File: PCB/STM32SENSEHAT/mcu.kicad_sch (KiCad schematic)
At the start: 3 parts, among them J2 Conn_01x24_Socket, J3 Conn_01x24_Socket, J6 Conn_01x10_Pin

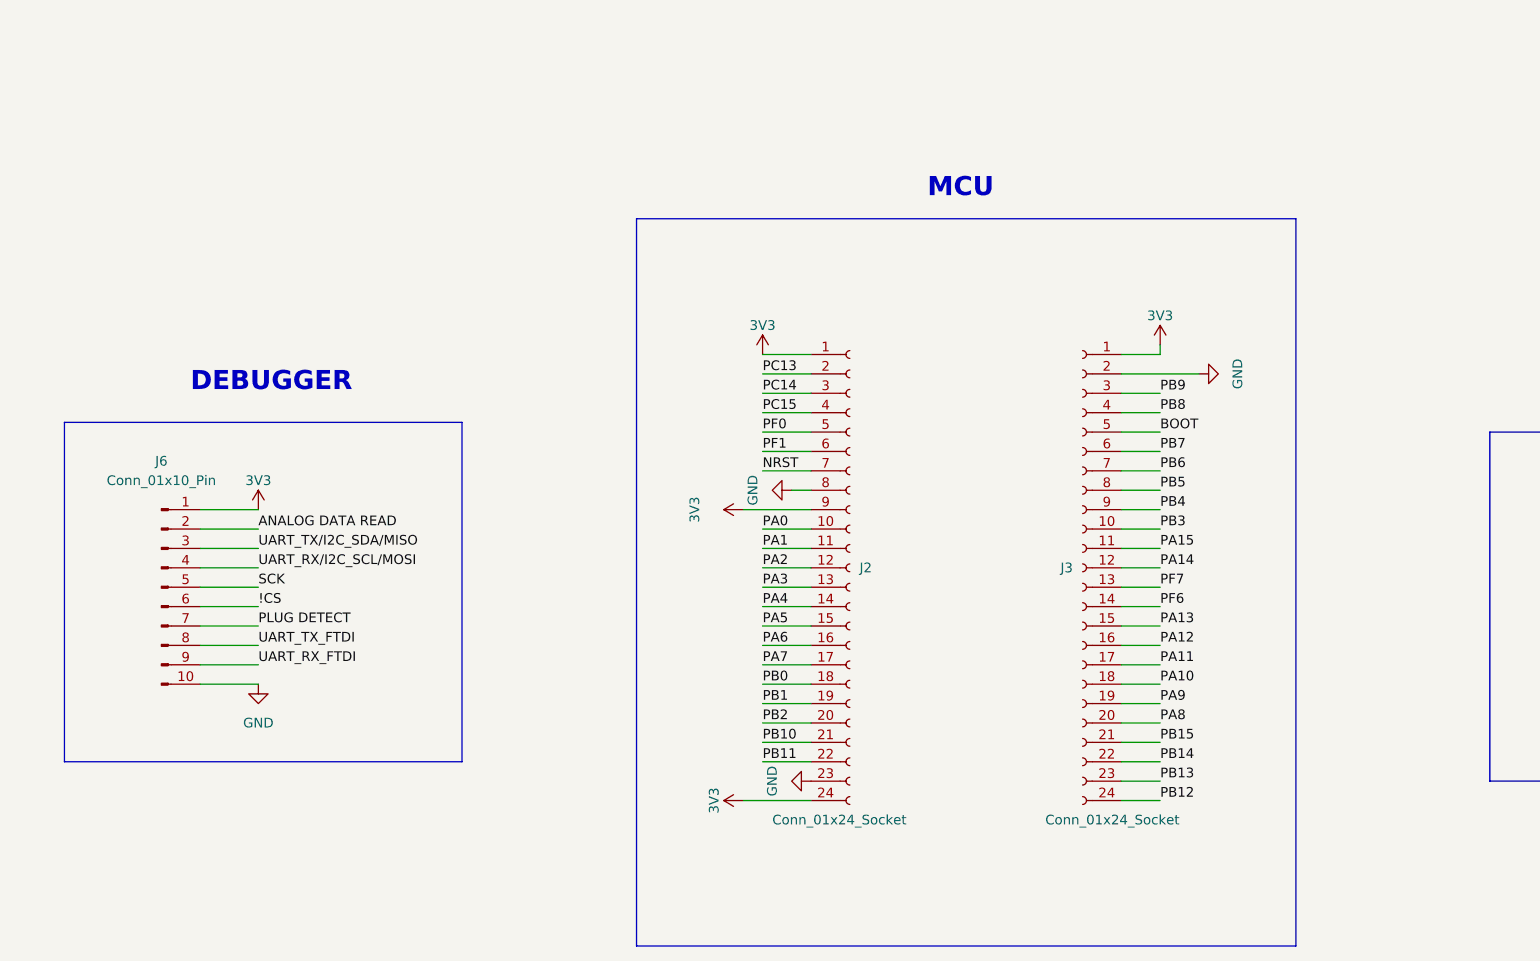
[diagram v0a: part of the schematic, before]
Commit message: Removed the extra sensor, Modified BME280 interfacing and FTDI UART pins. Added Manual Reset to MCU and configured BOOT pin
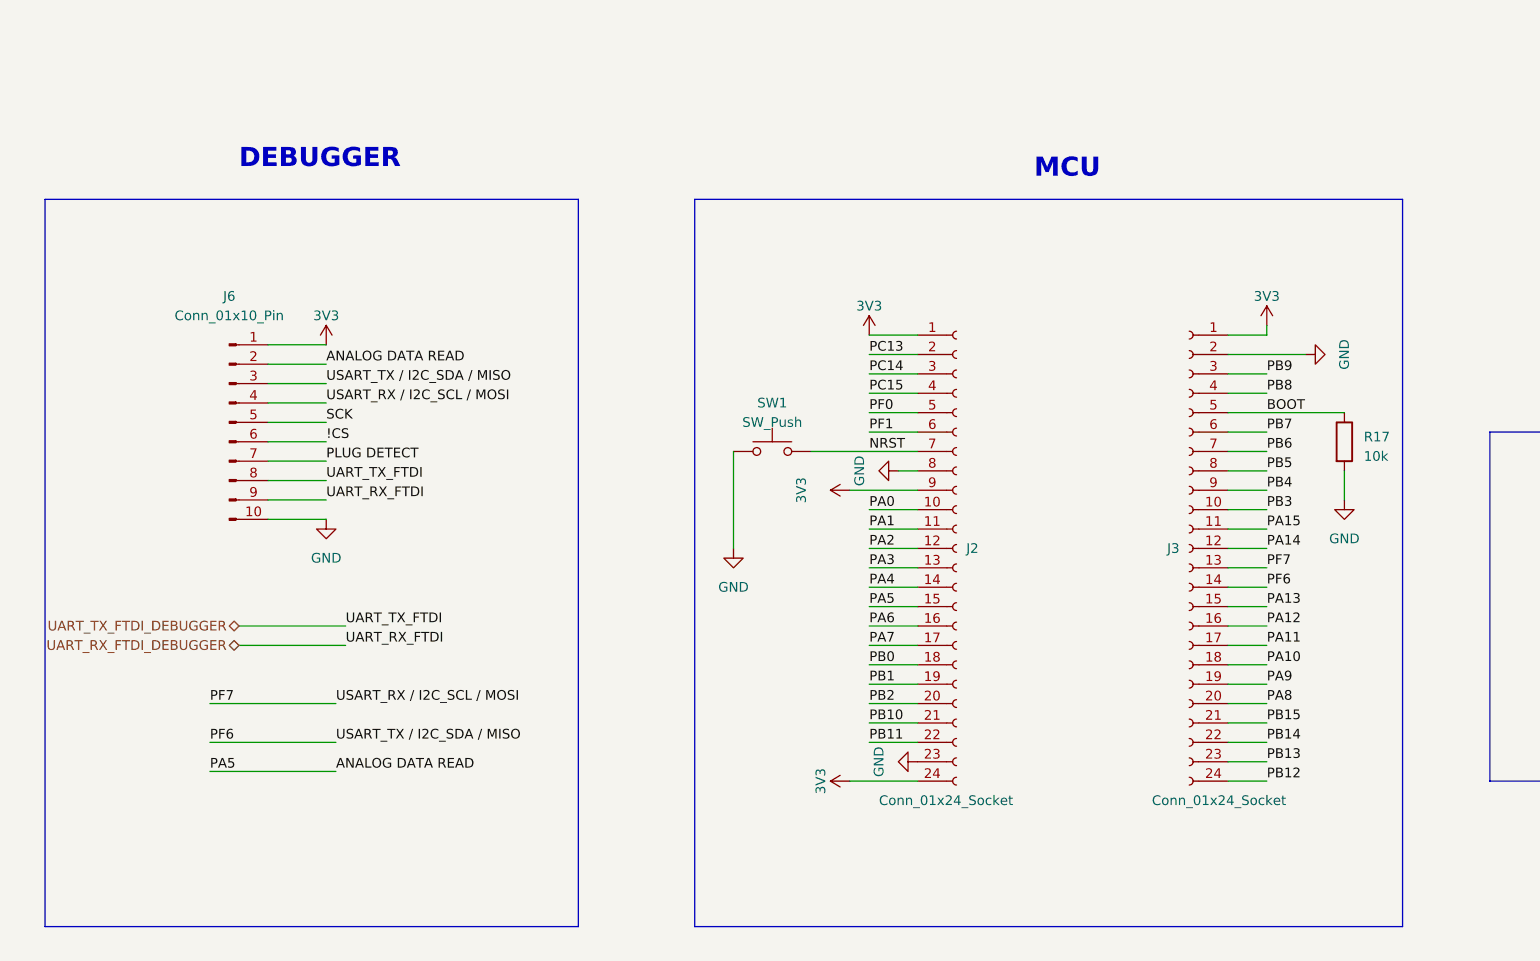
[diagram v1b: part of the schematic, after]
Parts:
- added R17: 10k, symbol Device:R
- added SW1: SW_Push, symbol Switch:SW_Push
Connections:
- net ANALOG DATA READ is gone; now on net PA5: J6.2 (Pin_2)
- net UART_RX/I2C_SCL/MOSI is gone; now on net STM_I2C_SCL: J6.4 (Pin_4)
- net UART_TX/I2C_SDA/MISO is gone; now on net STM_I2C_SDA: J6.3 (Pin_3)
- net BOOT: now also R17.1
- net GND: now also R17.2, SW1.1
- net NRST: now also SW1.2
- net UART_RX_FTDI renamed UART_RX_FTDI_DEBUGGER
- net UART_TX_FTDI renamed UART_TX_FTDI_DEBUGGER
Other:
- moved on the sheet: J2, J3, J6

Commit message: Revised schematics. Moved USB and EEPROM sub modules to MCU sheet and and rectified the top sheet accordingly
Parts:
- added C1, C2: 47pF, symbol Device:C_Small
- added C3: 10nF, symbol Device:C_Small
- added C4, C5: 100nF, symbol Device:C_Small
- added C6: 4.7uF, symbol Device:C_Small
- added FB1: FerriteBead, symbol Device:FerriteBead
- added J1: USB_B_Micro, symbol Connector:USB_B_Micro
- added J7: Conn_01x05_Pin, symbol Connector:Conn_01x05_Pin
- added R13, R16: 1.5k, symbol Device:R
- added R2, R3: 27R, symbol Device:R_Small
- added U3: FT230XQ, Package_DFN_QFN:QFN-16-1EP_4x4mm_P0.65mm_EP2.1x2.1mm, symbol Interface_USB:FT230XQ
- added U6: CAT24C256, symbol Memory_EEPROM:CAT24C256
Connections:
- net UART_RX_FTDI_DEBUGGER is gone; now on net PA10: J6.9 (Pin_9)
- net UART_TX_FTDI_DEBUGGER is gone; now on net PA9: J6.8 (Pin_8)
- net GND: now also C1.2, C2.2, C3.2, C4.2, C5.2, C6.2, J1.4 (ID), J1.5 (GND), J1.6 (Shield), J7.4 (Pin_4), J7.5 (Pin_5), U3.13 (GND), U3.17 (GND), U3.3 (GND), U6.1 (A0), U6.2 (A1), U6.3 (A2), U6.4 (GND), U6.7 (WP)
- net STM_I2C_SCL: now also R16.2, U6.6 (SCL)
- net STM_I2C_SDA: now also R13.2, U6.5 (SDA)
- net VCC: now also C3.1, C5.1, C6.1, FB1.1, FB1.2, J1.1 (VBUS), J7.1 (Pin_1), R13.1, R16.1, U3.10 (VCC), U6.8 (VCC)
- net STM_UART_RX renamed PA9
- net PA9: now also U3.15 (TXD)
- net STM_UART_TX renamed PA10
- net PA10: now also U3.2 (RXD)
- new net: C4.1, U3.1 (VCCIO), U3.8 (3V3OUT), U3.9 (~{RESET})
- new net: R3.2, U3.7 (USBDM)
- new net: R2.2, U3.6 (USBDP)
- new net CTS: U3.4 (~{CTS})
- new net D+: C2.1, J1.3 (D+), J7.3 (Pin_3), R2.1
- new net D-: C1.1, J1.2 (D-), J7.2 (Pin_2), R3.1
- new net RTS: U3.16 (~{RTS})
- no-connect marks 0 -> 4
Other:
- note added: "MEMORY"
- note added: "USB-FTDI INTERFACE"

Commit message: Added extra set of male pin headers
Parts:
- added J5, J8: Conn_01x24_Pin, symbol Connector:Conn_01x24_Pin
- added J7: Conn_01x04_Socket, symbol Connector:Conn_01x04_Socket
- added J9: Conn_01x05_Socket, symbol Connector:Conn_01x05_Socket
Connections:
- net BOOT: now also J5.5 (Pin_5)
- net GND: now also J5.2 (Pin_2), J8.23 (Pin_23), J8.8 (Pin_8), J9.5 (Pin_5)
- net NRST: now also J7.1 (Pin_1), J8.7 (Pin_7)
- net PA0: now also J8.10 (Pin_10)
- net PA1: now also J8.11 (Pin_11)
- net PA10: now also J5.18 (Pin_18)
- net PA11: now also J5.17 (Pin_17)
- net PA12: now also J5.16 (Pin_16)
- net PA13: now also J5.15 (Pin_15), J7.3 (Pin_3)
- net PA14: now also J5.12 (Pin_12), J7.2 (Pin_2)
- net PA15: now also J5.11 (Pin_11)
- net PA2: now also J8.12 (Pin_12)
- net PA3: now also J8.13 (Pin_13)
- net PA4: now also J8.14 (Pin_14)
- net PA5: now also J8.15 (Pin_15)
- net PA6: now also J8.16 (Pin_16)
- net PA7: now also J8.17 (Pin_17)
- net PA8: now also J5.20 (Pin_20)
- net PA9: now also J5.19 (Pin_19)
- net PB0: now also J8.18 (Pin_18)
- net PB1: now also J8.19 (Pin_19)
- net PB10: now also J8.21 (Pin_21)
- net PB11: now also J8.22 (Pin_22)
- net PB12: now also J5.24 (Pin_24)
- net PB13: now also J5.23 (Pin_23)
- net PB14: now also J5.22 (Pin_22)
- net PB15: now also J5.21 (Pin_21)
- net PB2: now also J8.20 (Pin_20)
- net PB3: now also J5.10 (Pin_10)
- net PB4: now also J5.9 (Pin_9)
- net PB5: now also J5.8 (Pin_8)
- net PB6: now also J5.7 (Pin_7)
- net PB7: now also J5.6 (Pin_6)
- net PB8: now also J5.4 (Pin_4)
- net PB9: now also J5.3 (Pin_3)
- net PC13: now also J8.2 (Pin_2)
- net PC14: now also J8.3 (Pin_3)
- net PC15: now also J8.4 (Pin_4)
- net PF0: now also J8.5 (Pin_5)
- net PF1: now also J8.6 (Pin_6)
- net STM_I2C_SCL: now also J5.13 (Pin_13)
- net STM_I2C_SDA: now also J5.14 (Pin_14)
- net VCC: now also J9.1 (Pin_1), J9.2 (Pin_2)
- net D+ renamed USB_DP
- net USB_DP: now also J9.3 (Pin_3)
- net D- renamed USB_DN
- net USB_DN: now also J9.4 (Pin_4)
- new net VBAT: J8.1 (Pin_1)
- new net VDD: J5.1 (Pin_1), J8.24 (Pin_24)
- new net VDDA: J8.9 (Pin_9)
- no-connect marks 4 -> 5
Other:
- note added: "TEST-P0INTS"
- moved on the sheet: C1, C2, C3, C4, C5, C6, FB1, J1, J2, J3, J6, J7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

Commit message: Protectuion features added to all schematica
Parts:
- added R14 (x2): 0R, symbol Device:R_Small
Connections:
- net STM_I2C_SCL: now also R14.2; no longer U6.6 (SCL)
- net STM_I2C_SDA: now also R14.1; no longer R13.2
- net VCC: no longer C3.1, FB1.2, J1.1 (VBUS), J2.1 (Pin_1), J2.24 (Pin_24), J2.9 (Pin_9), J3.1 (Pin_1), J6.1 (Pin_1), J7.1 (Pin_1), J9.1 (Pin_1), J9.2 (Pin_2), R13.1, R16.1, U6.8 (VCC)
- net CTS: no longer names the net of U3.4 (~{CTS})
- net RTS: no longer names the net of U3.16 (~{RTS})
- new net: R14.1, U6.6 (SCL)
- new net: R13.2, R14.2
- new net +5V: C3.1, FB1.2, J1.1 (VBUS), J7.1 (Pin_1), J9.1 (Pin_1)
- new net 3V3: J2.1 (Pin_1), J2.24 (Pin_24), J2.9 (Pin_9), J3.1 (Pin_1), J6.1 (Pin_1), J9.2 (Pin_2), R13.1, R16.1, U6.8 (VCC)
- no-connect marks 5 -> 7
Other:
- moved on the sheet: J2, J3, J5, J6, J7, J8, J9, R13, R16, R17, SW1, U6

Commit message: Schematics reviewed
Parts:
- J2, J3, J5, J8: footprint (none) -> Connector_PinHeader_2.54mm:PinHeader_1x24_P2.54mm_Vertical
- J6: footprint (none) -> Connector_PinHeader_2.54mm:PinHeader_1x10_P2.54mm_Vertical
- J7: footprint (none) -> Connector_PinHeader_2.54mm:PinHeader_1x04_P2.54mm_Vertical
- J7, J9: footprint (none) -> Connector_PinHeader_2.54mm:PinHeader_1x05_P2.54mm_Vertical
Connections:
- net VCC is gone; now on net +5V: C5.1, C6.1, FB1.1, U3.10 (VCC)
- net +5V: no longer C3.1, FB1.2, J1.1 (VBUS), J7.1 (Pin_1)
- net PB12 renamed STM32_CS
- net PB13 renamed STM32_SCLK
- net PB14 renamed STM32_MISO
- net PB15 renamed STM32_MOSI
- new net VBUS: C3.1, FB1.2, J1.1 (VBUS), J7.1 (Pin_1)

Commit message: Added footprints to the components but still pending review by Rumbizdai and Phomolo
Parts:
- C1, C2, C3, C4, C5, C6: footprint (none) -> Capacitor_SMD:C_0805_2012Metric
- FB1, R2, R3: footprint (none) -> Resistor_SMD:R_0603_1608Metric
- J1: footprint (none) -> Connector_USB:USB_Micro-AB_Molex_47590-0001
- J2, J3: footprint Connector_PinHeader_2.54mm:PinHeader_1x24_P2.54mm_Vertical -> Connector_PinSocket_2.54mm:PinSocket_1x24_P2.54mm_Vertical
- J7: footprint Connector_PinHeader_2.54mm:PinHeader_1x04_P2.54mm_Vertical -> Connector_PinSocket_2.54mm:PinSocket_1x04_P2.54mm_Vertical
- J9: footprint Connector_PinHeader_2.54mm:PinHeader_1x05_P2.54mm_Vertical -> Connector_PinSocket_2.54mm:PinSocket_1x05_P2.54mm_Vertical
- R13, R14, R16, R17: footprint (none) -> Resistor_SMD:R_0805_2012Metric
- SW1: footprint (none) -> Button_Switch_THT:SW_PUSH_6mm
- U6: footprint (none) -> Package_SO:SOIC-8-1EP_3.9x4.9mm_P1.27mm_EP2.41x3.3mm
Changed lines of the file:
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@@
       (effects (font (size 1.27 1.27)) (justify left))
     )
-    (property "Footprint" "Connector_PinHeader_2.54mm:PinHeader_1x24_P2.54mm_Vertical" (at 240.03 64.77 0)
+    (property "Footprint" "Connector_PinSocket_2.54mm:PinSocket_1x24_P2.54mm_Vertical" (at 240.03 64.77 0)
       (effects (font (size 1.27 1.27)) hide)
     )
@@
       (effects (font (size 1.27 1.27)) (justify left))
     )
-    (property "Footprint" "Connector_PinHeader_2.54mm:PinHeader_1x05_P2.54mm_Vertical" (at 118.11 64.77 0)
+    (property "Footprint" "Connector_PinSocket_2.54mm:PinSocket_1x05_P2.54mm_Vertical" (at 118.11 64.77 0)
       (effects (font (size 1.27 1.27)) hide)
     )
@@
       (effects (font (size 1.27 1.27)))
     )
-    (property "Footprint" "" (at 38.1 153.67 0)
+    (property "Footprint" "Connector_USB:USB_Micro-AB_Molex_47590-0001" (at 38.1 153.67 0)
       (effects (font (size 1.27 1.27)) hide)
     )
@@
       (effects (font (size 1.27 1.27)) (justify left))
     )
-    (property "Footprint" "" (at 258.572 50.8 90)
+    (property "Footprint" "Resistor_SMD:R_0805_2012Metric" (at 258.572 50.8 90)
       (effects (font (size 1.27 1.27)) hide)
     )
@@
       (effects (font (size 1.27 1.27)) (justify left))
     )
-    (property "Footprint" "" (at 92.71 182.88 0)
+    (property "Footprint" "Capacitor_SMD:C_0805_2012Metric" (at 92.71 182.88 0)
       (effects (font (size 1.27 1.27)) hide)
     )
@@
       (effects (font (size 1.27 1.27)) (justify left))
     )
-    (property "Footprint" "" (at 69.85 154.94 0)
+    (property "Footprint" "Resistor_SMD:R_0603_1608Metric" (at 69.85 154.94 0)
       (effects (font (size 1.27 1.27)) hide)
     )
@@
       (effects (font (size 1.27 1.27)))
     )
-    (property "Footprint" "" (at 355.6 66.04 0)
+    (property "Footprint" "Resistor_SMD:R_0805_2012Metric" (at 355.6 66.04 0)
       (effects (font (size 1.27 1.27)) hide)
     )
@@
       (effects (font (size 1.27 1.27)) (justify left))
     )
-    (property "Footprint" "" (at 332.74 66.04 0)
+    (property "Footprint" "Package_SO:SOIC-8-1EP_3.9x4.9mm_P1.27mm_EP2.41x3.3mm" (at 332.74 66.04 0)
       (effects (font (size 1.27 1.27)) hide)
     )
@@
       (effects (font (size 1.27 1.27)) (justify left))
     )
-    (property "Footprint" "" (at 53.34 171.45 0)
+    (property "Footprint" "Capacitor_SMD:C_0805_2012Metric" (at 53.34 171.45 0)
       (effects (font (size 1.27 1.27)) hide)
     )
@@
       (effects (font (size 1.27 1.27)) (justify left))
     )
-    (property "Footprint" "" (at 50.8 203.2 0)
+    (property "Footprint" "Capacitor_SMD:C_0805_2012Metric" (at 50.8 203.2 0)
       (effects (font (size 1.27 1.27)) hide)
     )
@@
       (effects (font (size 1.27 1.27)) (justify left))
     )
-    (property "Footprint" "Connector_PinHeader_2.54mm:PinHeader_1x04_P2.54mm_Vertical" (at 135.89 63.5 0)
+    (property "Footprint" "Connector_PinSocket_2.54mm:PinSocket_1x04_P2.54mm_Vertical" (at 135.89 63.5 0)
       (effects (font (size 1.27 1.27)) hide)
     )
@@
       (effects (font (size 1.27 1.27)) (justify left))
     )
-    (property "Footprint" "" (at 33.02 203.2 0)
+    (property "Footprint" "Capacitor_SMD:C_0805_2012Metric" (at 33.02 203.2 0)
       (effects (font (size 1.27 1.27)) hide)
     )
@@
       (effects (font (size 1.27 1.27)) (justify left))
     )
-    (property "Footprint" "" (at 61.722 132.08 90)
+    (property "Footprint" "Resistor_SMD:R_0603_1608Metric" (at 61.722 132.08 90)
       (effects (font (size 1.27 1.27)) hide)
     )
@@
       (effects (font (size 1.27 1.27)))
     )
-    (property "Footprint" "" (at 200.66 46.99 0)
+    (property "Footprint" "Button_Switch_THT:SW_PUSH_6mm" (at 200.66 46.99 0)
       (effects (font (size 1.27 1.27)) hide)
     )
@@
       (effects (font (size 1.27 1.27)) (justify right))
     )
-    (property "Footprint" "" (at 359.41 58.42 0)
+    (property "Footprint" "Resistor_SMD:R_0805_2012Metric" (at 359.41 58.42 0)
       (effects (font (size 1.27 1.27)) hide)
     )
@@
       (effects (font (size 1.27 1.27)) (justify left))
     )
-    (property "Footprint" "" (at 64.77 171.45 0)
+    (property "Footprint" "Capacitor_SMD:C_0805_2012Metric" (at 64.77 171.45 0)
       (effects (font (size 1.27 1.27)) hide)
     )
@@
       (effects (font (size 1.27 1.27)) (justify left))
     )
-    (property "Footprint" "Connector_PinHeader_2.54mm:PinHeader_1x24_P2.54mm_Vertical" (at 224.79 64.77 0)
+    (property "Footprint" "Connector_PinSocket_2.54mm:PinSocket_1x24_P2.54mm_Vertical" (at 224.79 64.77 0)
       (effects (font (size 1.27 1.27)) hide)
     )
@@
       (effects (font (size 1.27 1.27)) (justify left))
     )
-    (property "Footprint" "" (at 369.062 57.15 90)
+    (property "Footprint" "Resistor_SMD:R_0805_2012Metric" (at 369.062 57.15 90)
       (effects (font (size 1.27 1.27)) hide)
     )
@@
       (effects (font (size 1.27 1.27)) (justify left))
     )
-    (property "Footprint" "" (at 357.632 50.8 90)
+    (property "Footprint" "Resistor_SMD:R_0805_2012Metric" (at 357.632 50.8 90)
       (effects (font (size 1.27 1.27)) hide)
     )
@@
       (effects (font (size 1.27 1.27)) (justify left))
     )
-    (property "Footprint" "" (at 69.85 152.4 0)
+    (property "Footprint" "Resistor_SMD:R_0603_1608Metric" (at 69.85 152.4 0)
       (effects (font (size 1.27 1.27)) hide)
     )
@@
       (effects (font (size 1.27 1.27)) (justify left))
     )
-    (property "Footprint" "" (at 45.72 161.29 0)
-      (effects (font (size 1.27 1.27)) hide)
-    )
+    (property "Footprint" "Capacitor_SMD:C_0805_2012Metric" (at 45.72 161.29 0)
+      (effects (font (size 1.27 1.27)) hide)
+    )
